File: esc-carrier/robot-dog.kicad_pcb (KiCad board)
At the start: 2 copper layers, 74.3 x 78.1 mm, 35 parts, among them J1 Conn_01x02, J10 Conn_01x02, J11 Conn_01x04, J12 Conn_01x04, J13 Conn_01x04, J2 Conn_01x04, J3 Conn_01x04, J4 Conn_01x03, J5 Conn_01x05, J6 Conn_01x05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

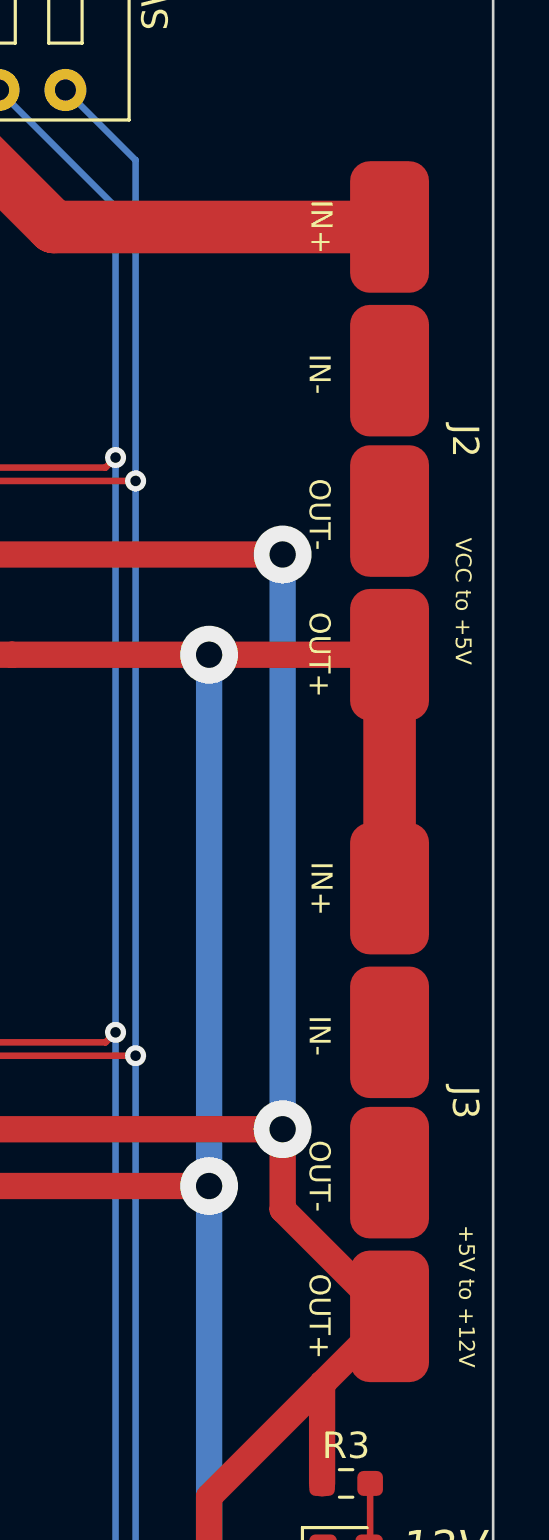
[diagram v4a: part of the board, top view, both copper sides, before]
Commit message: make voltage converter footprints tht
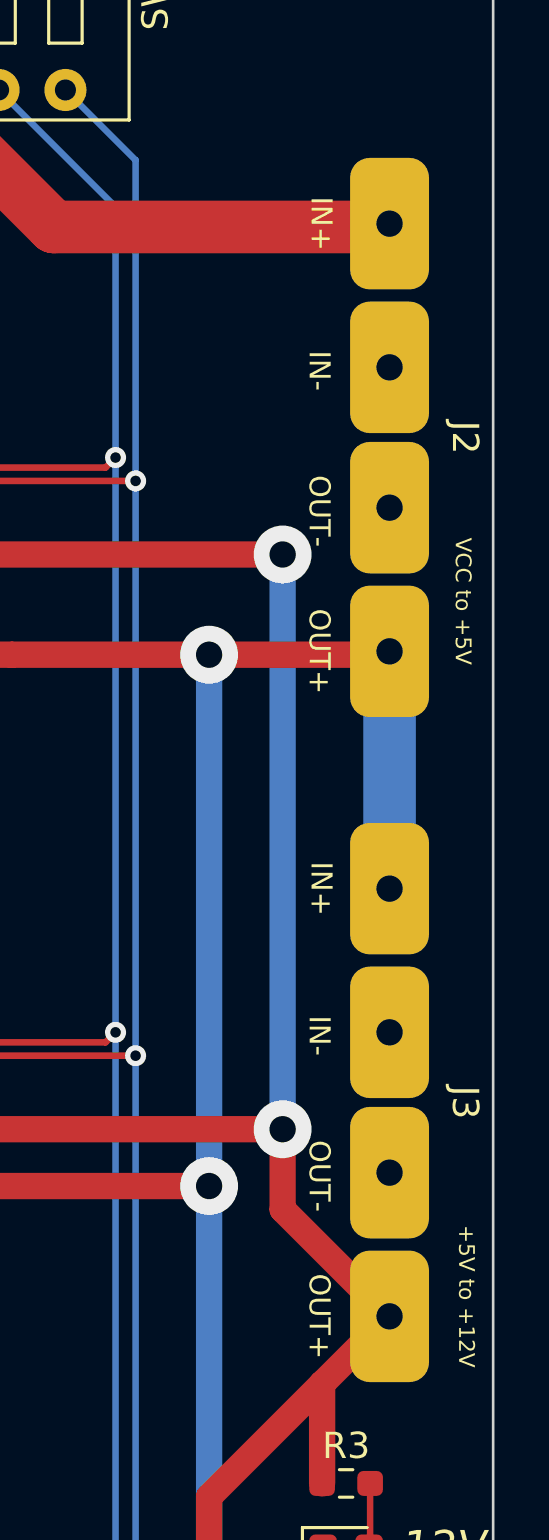
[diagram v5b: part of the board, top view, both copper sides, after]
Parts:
- moved J2 0.13 mm to (211.6, 59.3)
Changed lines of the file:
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@@
       (net 1 "VCC") (pinfunction "Pin_2") (pintype "passive") (zone_connect 2))
+  )
+  (footprint "DogESCCarrier:VoltageConverter1" (layer "F.Cu")
+    (at 211.582 59.309 -90)
+    (property "Sheetfile" "robot-dog.kicad_sch")
+    (property "Sheetname" "")
+    (attr smd)
+    (fp_text reference "J2" (at 0 -2.873 -90 unlocked) (layer "F.SilkS")
+      (effects (font (size 1 1) (thickness 0.15)))
+    )
+    (fp_text value "Conn_01x04" (at 0 4.342 -90 unlocked) (layer "F.Fab")
+      (effects (font (size 1 1) (thickness 0.15)))
+    )
+    (fp_text user "IN-" (at -2.54 2.667 -90 unlocked) (layer "F.SilkS")
+      (effects (font (size 0.8 0.8) (thickness 0.15)))
+    )
+    (fp_text user "OUT-" (at 2.794 2.667 -90 unlocked) (layer "F.SilkS")
+      (effects (font (size 0.8 0.8) (thickness 0.15)))
+    )
+    (fp_text user "IN+" (at -8.128 2.594 -90 unlocked) (layer "F.SilkS")
+      (effects (font (size 0.8 0.8) (thickness 0.15)))
+    )
+    (fp_text user "OUT+" (at 8.128 2.667 -90 unlocked) (layer "F.SilkS")
+      (effects (font (size 0.8 0.8) (thickness 0.15)))
+    )
+    (fp_text user "${REFERENCE}" (at 0 5.842 -90 unlocked) (layer "F.Fab")
+      (effects (font (size 1 1) (thickness 0.15)))
+    )
+    (fp_rect (start -10.922 -1.905) (end 10.922 1.905) (layer "F.CrtYd") (width 0.12) (fill none))
+    (pad "1" thru_hole roundrect (at -8.128 0 270) (size 5 3) (drill 1) (layers *.Cu *.Mask) (roundrect_rratio 0.25)
+      (net 1 "VCC") (pinfunction "Pin_1") (pintype "passive") (zone_connect 2))
+    (pad "2" thru_hole roundrect (at -2.667 0 270) (size 5 3) (drill 1) (layers *.Cu *.Mask) (roundrect_rratio 0.25)
+      (net 2 "GND") (pinfunction "Pin_2") (pintype "passive") (zone_connect 2))
+    (pad "3" thru_hole roundrect (at 2.667 0 270) (size 5 3) (drill 1) (layers *.Cu *.Mask) (roundrect_rratio 0.25)
+      (net 2 "GND") (pinfunction "Pin_3") (pintype "passive") (zone_connect 2))
+    (pad "4" thru_hole roundrect (at 8.128 0 270) (size 5 3) (drill 1) (layers *.Cu *.Mask) (roundrect_rratio 0.25)
+      (net 6 "+5V") (pinfunction "Pin_4") (pintype "passive") (zone_connect 2))
   )
   (footprint "Connector_AMASS:AMASS_XT60-M_1x02_P7.20mm_Vertical" (layer "F.Cu")
@@
   )
   (footprint "DogESCCarrier:VoltageConverter1" (layer "F.Cu")
-    (at 211.582 59.436 -90)
-    (property "Sheetfile" "robot-dog.kicad_sch")
-    (property "Sheetname" "")
-    (attr smd)
-    (fp_text reference "J2" (at 0 -2.873 -90 unlocked) (layer "F.SilkS")
+    (at 211.582 84.582 -90)
+    (property "Sheetfile" "robot-dog.kicad_sch")
+    (property "Sheetname" "")
+    (attr smd)
+    (fp_text reference "J3" (at 0 -2.873 -90 unlocked) (layer "F.SilkS")
       (effects (font (size 1 1) (thickness 0.15)))
     )
     (fp_text value "Conn_01x04" (at 0 4.342 -90 unlocked) (layer "F.Fab")
       (effects (font (size 1 1) (thickness 0.15)))
+    )
+    (fp_text user "IN+" (at -8.128 2.594 -90 unlocked) (layer "F.SilkS")
+      (effects (font (size 0.8 0.8) (thickness 0.15)))
     )
     (fp_text user "OUT+" (at 8.128 2.667 -90 unlocked) (layer "F.SilkS")
@@
       (effects (font (size 0.8 0.8) (thickness 0.15)))
     )
-    (fp_text user "IN+" (at -8.128 2.594 -90 unlocked) (layer "F.SilkS")
-      (effects (font (size 0.8 0.8) (thickness 0.15)))
-    )
     (fp_text user "IN-" (at -2.54 2.667 -90 unlocked) (layer "F.SilkS")
       (effects (font (size 0.8 0.8) (thickness 0.15)))
@@
     )
     (fp_rect (start -10.922 -1.905) (end 10.922 1.905) (layer "F.CrtYd") (width 0.12) (fill none))
-    (pad "1" smd roundrect (at -8.128 0 270) (size 5 3) (layers "F.Cu" "F.Paste" "F.Mask") (roundrect_rratio 0.25)
-      (net 1 "VCC") (pinfunction "Pin_1") (pintype "passive"))
-    (pad "2" smd roundrect (at -2.667 0 270) (size 5 3) (layers "F.Cu" "F.Paste" "F.Mask") (roundrect_rratio 0.25)
+    (pad "1" thru_hole roundrect (at -8.128 0 270) (size 5 3) (drill 1) (layers *.Cu *.Mask) (roundrect_rratio 0.25)
+      (net 6 "+5V") (pinfunction "Pin_1") (pintype "passive") (zone_connect 2))
+    (pad "2" thru_hole roundrect (at -2.667 0 270) (size 5 3) (drill 1) (layers *.Cu *.Mask) (roundrect_rratio 0.25)
       (net 2 "GND") (pinfunction "Pin_2") (pintype "passive") (zone_connect 2))
-    (pad "3" smd roundrect (at 2.667 0 270) (size 5 3) (layers "F.Cu" "F.Paste" "F.Mask") (roundrect_rratio 0.25)
+    (pad "3" thru_hole roundrect (at 2.667 0 270) (size 5 3) (drill 1) (layers *.Cu *.Mask) (roundrect_rratio 0.25)
       (net 2 "GND") (pinfunction "Pin_3") (pintype "passive") (zone_connect 2))
-    (pad "4" smd roundrect (at 8.128 0 270) (size 5 3) (layers "F.Cu" "F.Paste" "F.Mask") (roundrect_rratio 0.25)
-      (net 6 "+5V") (pinfunction "Pin_4") (pintype "passive"))
+    (pad "4" thru_hole roundrect (at 8.128 0 270) (size 5 3) (drill 1) (layers *.Cu *.Mask) (roundrect_rratio 0.25)
+      (net 7 "+12V") (pinfunction "Pin_4") (pintype "passive") (zone_connect 2))
   )
   (footprint "DogESCCarrier:ESC-I2C-Pads" (layer "F.Cu")
@@
     (pad "5" smd roundrect (at 8 0) (size 1.5 3.2) (layers "F.Cu" "F.Paste" "F.Mask") (roundrect_rratio 0.25)
       (net 7 "+12V") (pinfunction "Pin_5") (pintype "passive"))
-  )
-  (footprint "DogESCCarrier:VoltageConverter1" (layer "F.Cu")
-    (at 211.582 84.582 -90)
-    (property "Sheetfile" "robot-dog.kicad_sch")
-    (property "Sheetname" "")
-    (attr smd)
-    (fp_text reference "J3" (at 0 -2.873 -90 unlocked) (layer "F.SilkS")
-      (effects (font (size 1 1) (thickness 0.15)))
-    )
-    (fp_text value "Conn_01x04" (at 0 4.342 -90 unlocked) (layer "F.Fab")
-      (effects (font (size 1 1) (thickness 0.15)))
-    )
-    (fp_text user "IN-" (at -2.54 2.667 -90 unlocked) (layer "F.SilkS")
-      (effects (font (size 0.8 0.8) (thickness 0.15)))
-    )
-    (fp_text user "OUT-" (at 2.794 2.667 -90 unlocked) (layer "F.SilkS")
-      (effects (font (size 0.8 0.8) (thickness 0.15)))
-    )
-    (fp_text user "OUT+" (at 8.128 2.667 -90 unlocked) (layer "F.SilkS")
-      (effects (font (size 0.8 0.8) (thickness 0.15)))
-    )
-    (fp_text user "IN+" (at -8.128 2.594 -90 unlocked) (layer "F.SilkS")
-      (effects (font (size 0.8 0.8) (thickness 0.15)))
-    )
-    (fp_text user "${REFERENCE}" (at 0 5.842 -90 unlocked) (layer "F.Fab")
-      (effects (font (size 1 1) (thickness 0.15)))
-    )
-    (fp_rect (start -10.922 -1.905) (end 10.922 1.905) (layer "F.CrtYd") (width 0.12) (fill none))
-    (pad "1" smd roundrect (at -8.128 0 270) (size 5 3) (layers "F.Cu" "F.Paste" "F.Mask") (roundrect_rratio 0.25)
-      (net 6 "+5V") (pinfunction "Pin_1") (pintype "passive"))
-    (pad "2" smd roundrect (at -2.667 0 270) (size 5 3) (layers "F.Cu" "F.Paste" "F.Mask") (roundrect_rratio 0.25)
-      (net 2 "GND") (pinfunction "Pin_2") (pintype "passive") (zone_connect 2))
-    (pad "3" smd roundrect (at 2.667 0 270) (size 5 3) (layers "F.Cu" "F.Paste" "F.Mask") (roundrect_rratio 0.25)
-      (net 2 "GND") (pinfunction "Pin_3") (pintype "passive") (zone_connect 2))
-    (pad "4" smd roundrect (at 8.128 0 270) (size 5 3) (layers "F.Cu" "F.Paste" "F.Mask") (roundrect_rratio 0.25)
-      (net 7 "+12V") (pinfunction "Pin_4") (pintype "passive"))
   )
   (footprint "DogESCCarrier:ESC-Power-Tabs" (layer "F.Cu")
@@
   (segment (start 204.724 87.757) (end 175.387 87.757) (width 1) (layer "F.Cu") (net 6))
   (segment (start 206.582 109.347) (end 208.995 106.934) (width 1) (layer "F.Cu") (net 6))
-  (segment (start 211.582 67.564) (end 211.582 76.454) (width 2) (layer "F.Cu") (net 6))
   (segment (start 172.085 100.995) (end 172.116 100.964) (width 1) (layer "F.Cu") (net 6))
   (segment (start 204.724 67.564) (end 197.231 67.564) (width 1) (layer "F.Cu") (net 6))
@@
   (via (at 204.724 87.757) (size 2.2) (drill 1) (layers "F.Cu" "B.Cu") (net 6))
   (segment (start 204.724 87.757) (end 204.724 67.564) (width 1) (layer "B.Cu") (net 6))
+  (segment (start 211.582 67.564) (end 211.582 76.454) (width 2) (layer "B.Cu") (net 6))
   (segment (start 204.724 87.757) (end 204.724 109.347) (width 1) (layer "B.Cu") (net 6))
   (segment (start 207.518 88.646) (end 207.518 85.598) (width 1) (layer "F.Cu") (net 7))

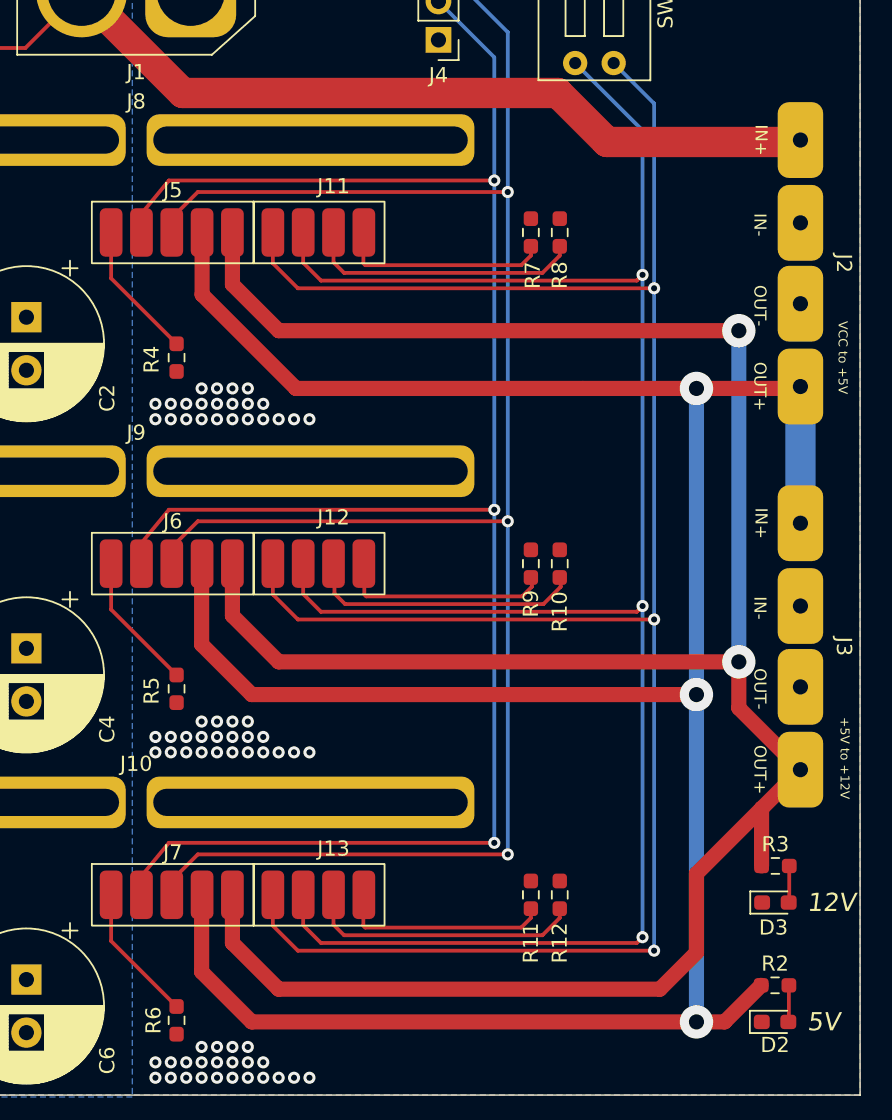
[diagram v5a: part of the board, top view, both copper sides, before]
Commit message: adjust control board pos
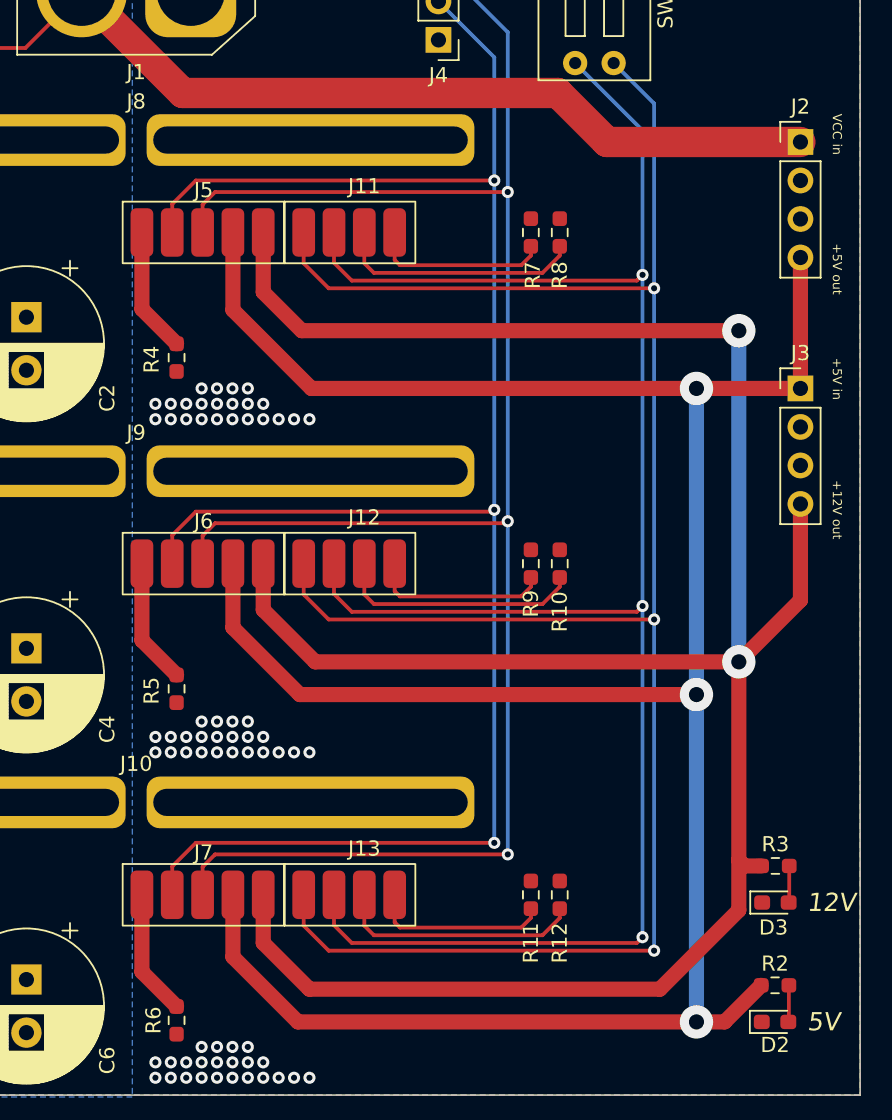
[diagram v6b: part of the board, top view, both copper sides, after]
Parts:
- J2, J3: footprint DogESCCarrier:VoltageConverter1 -> Connector_PinHeader_2.54mm:PinHeader_1x04_P2.54mm_Vertical
- moved J3 17.0 mm to (211.6, 67.6), turned to 0 degrees
- moved J2 8.00 mm to (211.6, 51.3), turned to 0 degrees
- moved J11 2.03 mm to (178.8, 57.3)
- moved J12 2.03 mm to (178.8, 79.1)
- moved J13 2.03 mm to (178.8, 101.0)
- moved J5 2.03 mm to (168.1, 57.3)
- moved J6 2.03 mm to (168.1, 79.1)
- moved J7 2.03 mm to (168.1, 101.0)
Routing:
- net +5V: track 180.3 -> 173.5 mm
- net Net-(J11-Pad1): track 143.2 -> 137.1 mm
- net Net-(J11-Pad2): track 134.6 -> 128.5 mm
- net SCL: track 133.7 -> 128.3 mm
- net SDA: track 132.2 -> 127.6 mm
- net Net-(J11-Pad4): track 14.0 -> 11.8 mm
- net Net-(J13-Pad4): track 14.0 -> 11.8 mm
- net Net-(J12-Pad4): track 14.0 -> 11.8 mm
- net Net-(J13-Pad3): track 18.3 -> 16.3 mm
- net Net-(J12-Pad3): track 18.3 -> 16.3 mm
- net Net-(J11-Pad3): track 18.3 -> 16.3 mm
- net +12V: track 161.3 -> 162.1 mm
- net Net-(J7-Pad1): track 9.16 -> 8.31 mm
- net Net-(J6-Pad1): track 9.13 -> 8.29 mm
- net Net-(J5-Pad1): track 9.13 -> 8.29 mm
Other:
- board text added: "+12V out"
- board text added: "+5V in"
- board text added: "+5V out"
- board text added: "VCC in"
- board text removed: "+5V to +12V"
- board text removed: "VCC to +5V"
